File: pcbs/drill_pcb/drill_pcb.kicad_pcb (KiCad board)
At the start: 2 copper layers, 105 x 103 mm, 41 parts, among them J1 24V IN, J11 STEPPER STORAGE, J13 uC COMMUNICATION, J14 SERVO 1, J15 SERVO 2, J16 DEEP WEIGHT SENSOR, J17 SURFACE WEIGHT SENSOR, J2 DC MOTOR 24 V, J3 DC MOTOR UART, J4 ENCODER VERTICAL DRIVE, J5 LIMIT SENSOR TOP, J6 HEIGHT SENSOR, J7 STEPPER VERTICAL DRIVE, J8 ENCODER STORAGE, J9 LIMIT SENSOR BOTTOM, Q1 PMOS, U1 ESP32-DevKitC, U2 LM3940, U3 INA219BxD

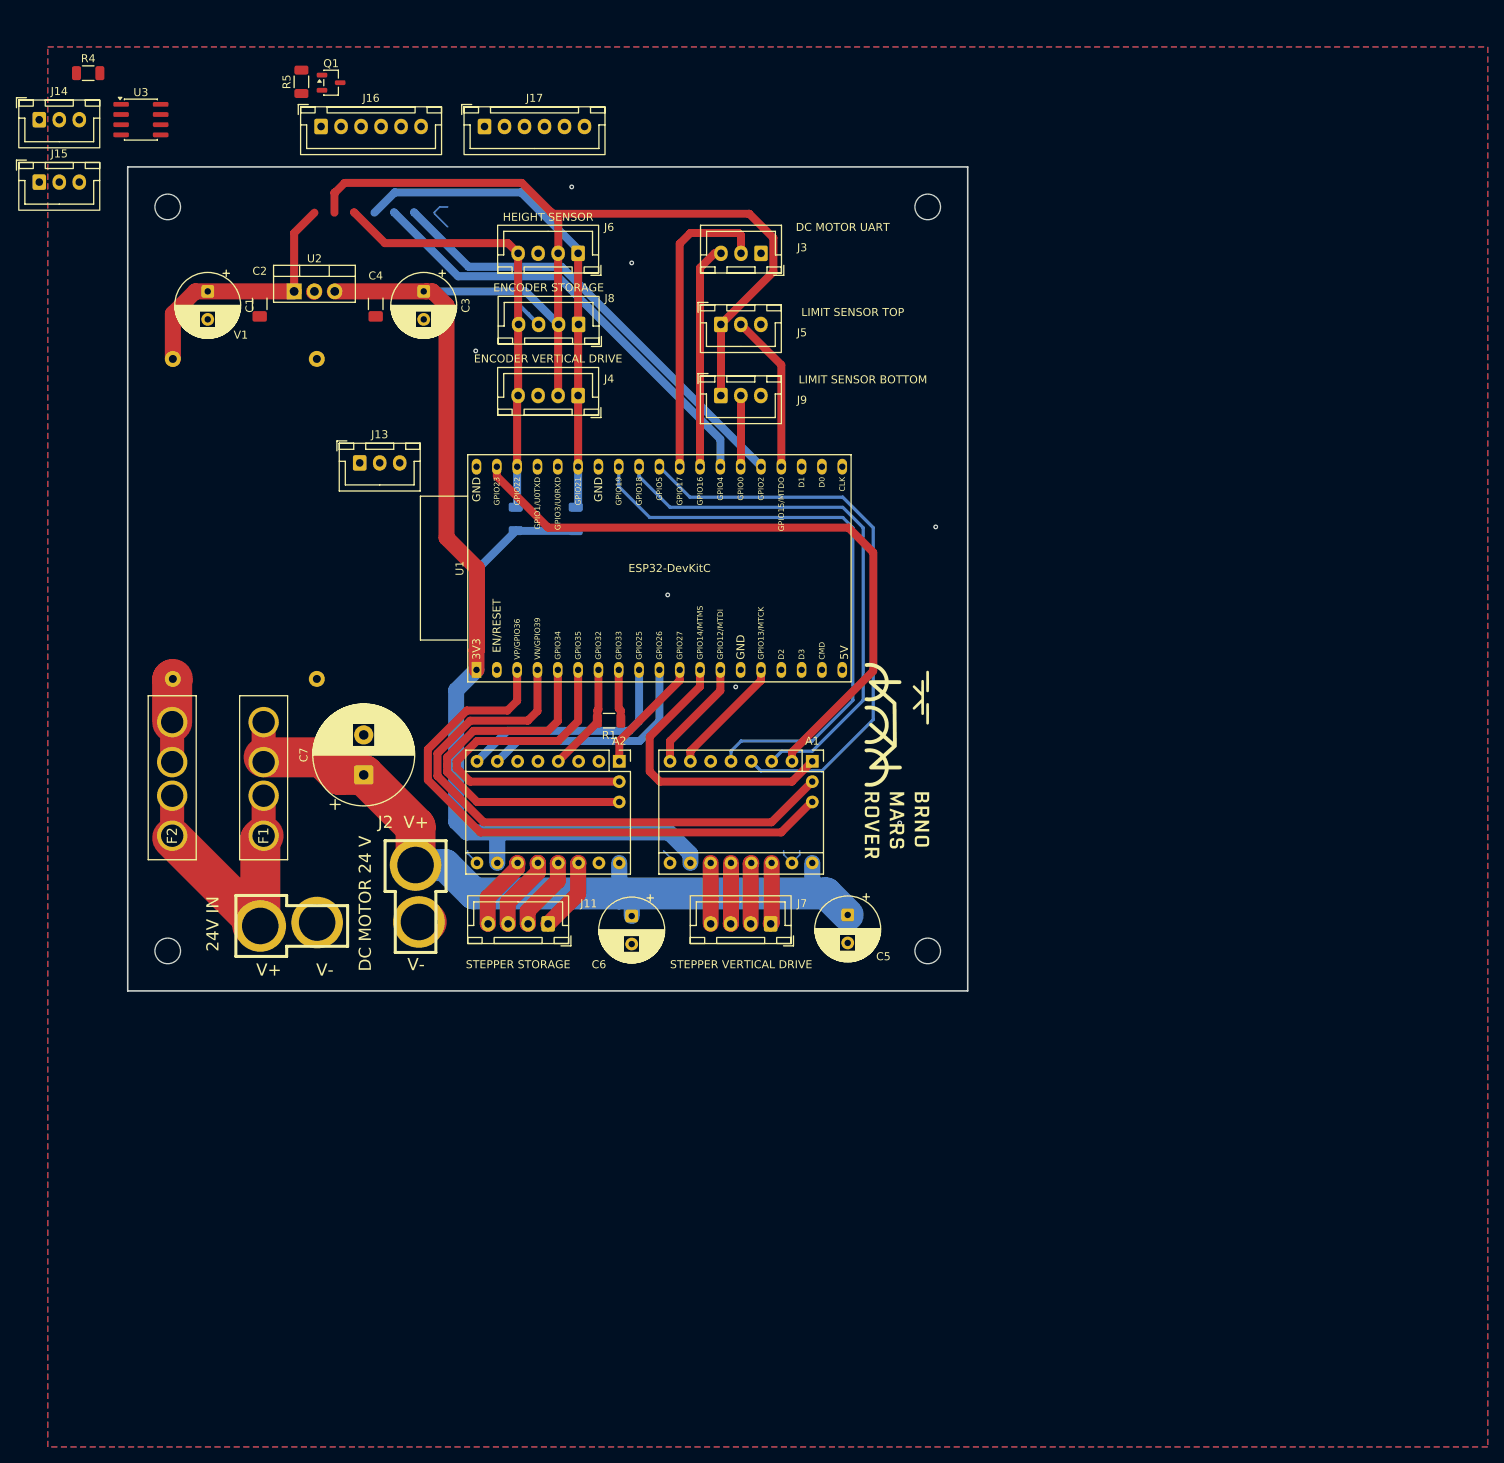
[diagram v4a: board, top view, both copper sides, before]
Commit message: Schematic changes: - Finalised the feature to turn off power for peripherals using a MOSFET. - Connected the stepper motor current sensor.
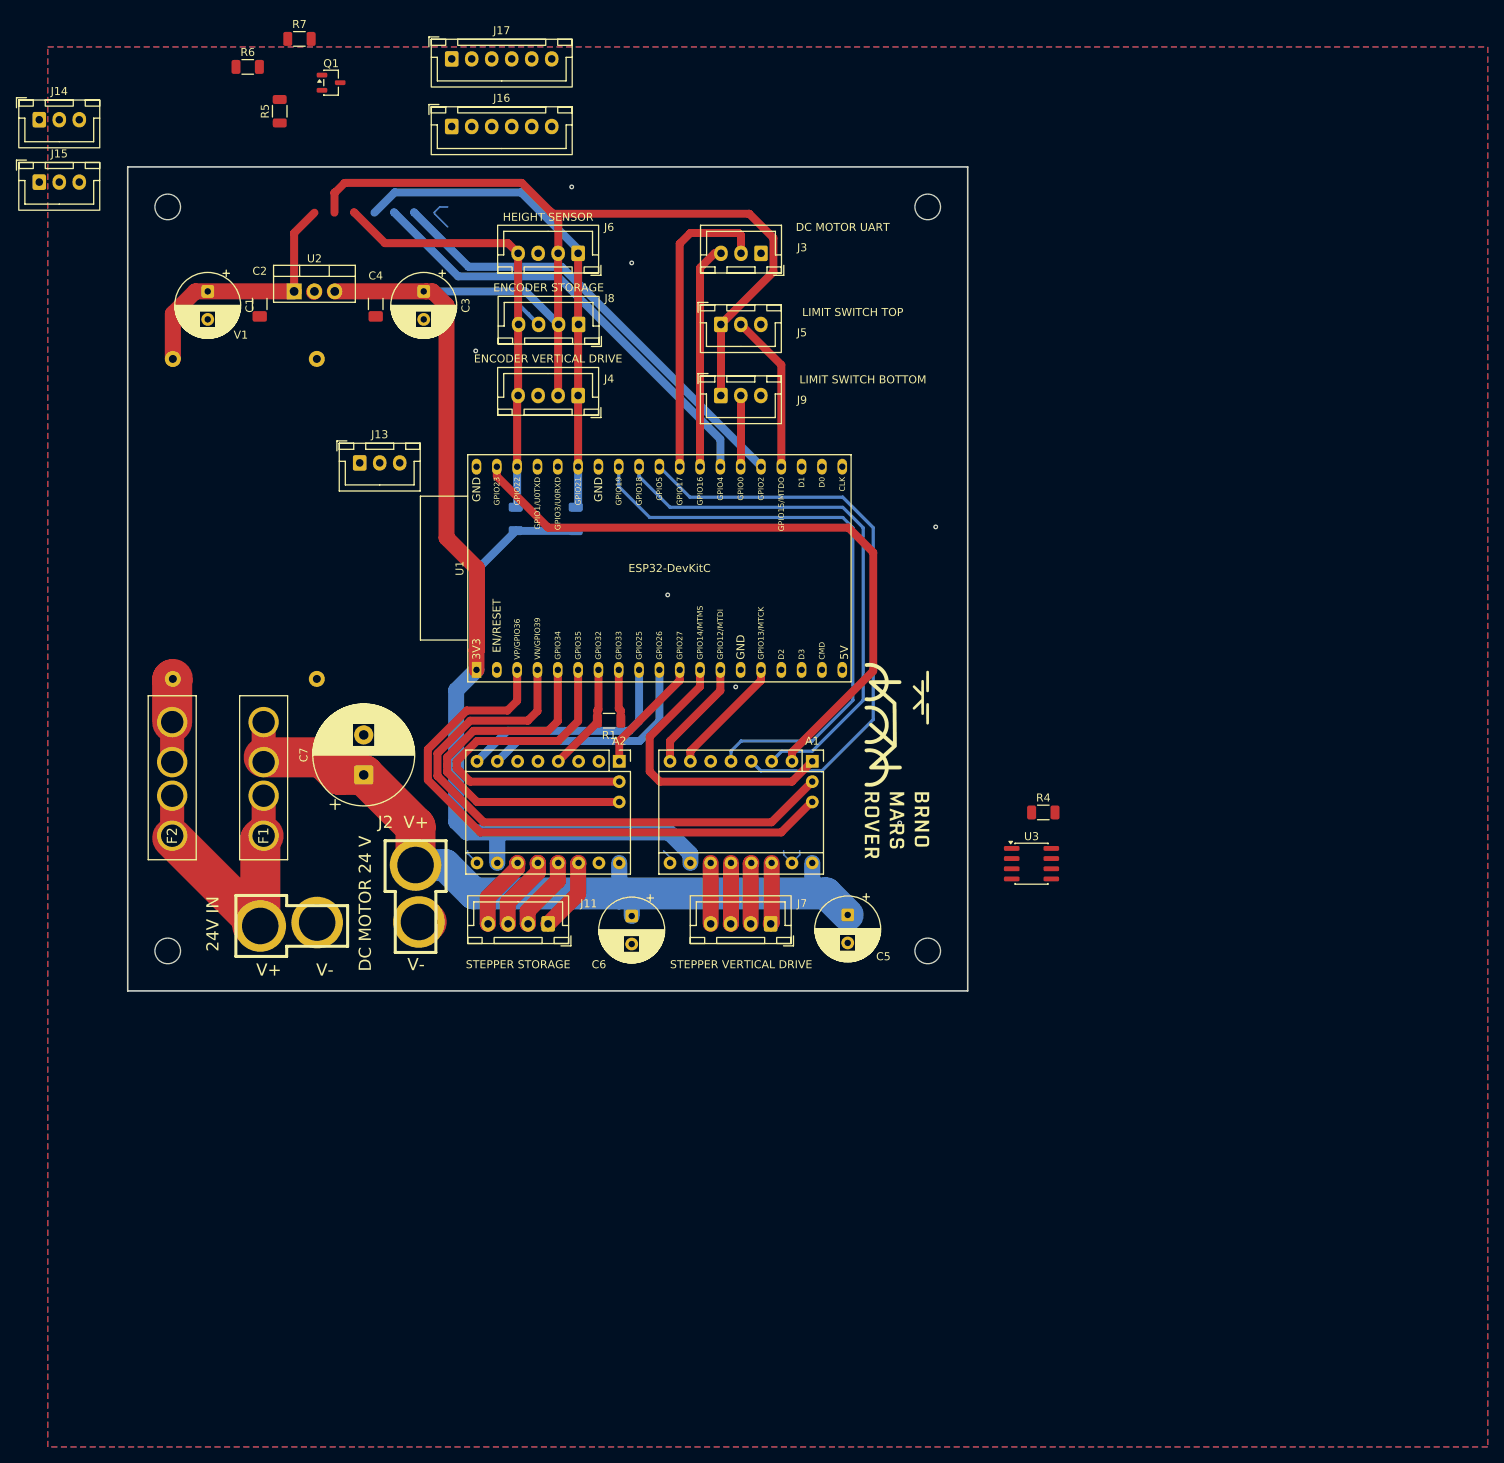
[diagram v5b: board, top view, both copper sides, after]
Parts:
- added R6: 100k, Resistor_SMD:R_1206_3216Metric, F.Cu at (45.0, 27.5)
- added R7: 1k, Resistor_SMD:R_1206_3216Metric, F.Cu at (51.5, 24.0)
- J5: value LIMIT SENSOR TOP -> LIMIT SWITCH TOP
- J9: value LIMIT SENSOR BOTTOM -> LIMIT SWITCH BOTTOM
- R4: value R -> R100
- R5: value R -> 100k
- moved R4 151.0 mm to (144.4, 120.7)
- moved U3 145.1 mm to (143.0, 127.1)
- moved J16 16.3 mm to (70.5, 35.0)
- moved J17 9.39 mm to (70.5, 26.5)
- moved R5 4.57 mm to (49.0, 33.0)
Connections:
- net LIMIT_SENSOR_BOTTOM renamed LIMIT_SWITCH_BOTTOM
- net LIMIT_SENSOR_TOP renamed LIMIT_SWITCH_TOP
- A1 pad 16: +24V -> Net-(A1-VM)
- C5 pad 1: +24V -> Net-(A1-VM)
- J16 pad 2: Net-(J16-Pin_2) -> RST
- J17 pad 2: Net-(J16-Pin_2) -> RST
- J4 pad 2: +3.3V -> +3.3VP
- J6 pad 2: +3.3V -> +3.3VP
- J8 pad 2: +3.3V -> +3.3VP
- Q1 pad 1: RST -> Net-(Q1-G)
- Q1 pad 3: Net-(J16-Pin_2) -> +3.3VP
- R4 pad 1: unconnected-(R4-Pad1) -> +24V
- R4 pad 2: unconnected-(R4-Pad2) -> Net-(A1-VM)
- R5 pad 2: RST -> Net-(Q1-G)
- U3 pad 5: +3.3V -> +3.3VP
- U3 pad 7: unconnected-(U3-IN--Pad7) -> Net-(A1-VM)
- U3 pad 8: unconnected-(U3-IN+-Pad8) -> +24V
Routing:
- net LIMIT_SWITCH_TOP: track 65.4 -> 0.00 mm
- net LIMIT_SWITCH_BOTTOM: track 55.9 -> 0.00 mm
- net unconnected-(A2-DIAG1-Pad18): track 0.00 -> 47.0 mm
- net unconnected-(A2-DIAG0-Pad17): track 0.00 -> 45.5 mm
- net unconnected-(U1-MTDO/GPIO15/ADC2_CH3-Pad23): track 0.00 -> 19.9 mm
- net unconnected-(U1-GPIO0/BOOT/ADC2_CH1-Pad25): track 0.00 -> 8.91 mm

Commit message: added servo capacitors
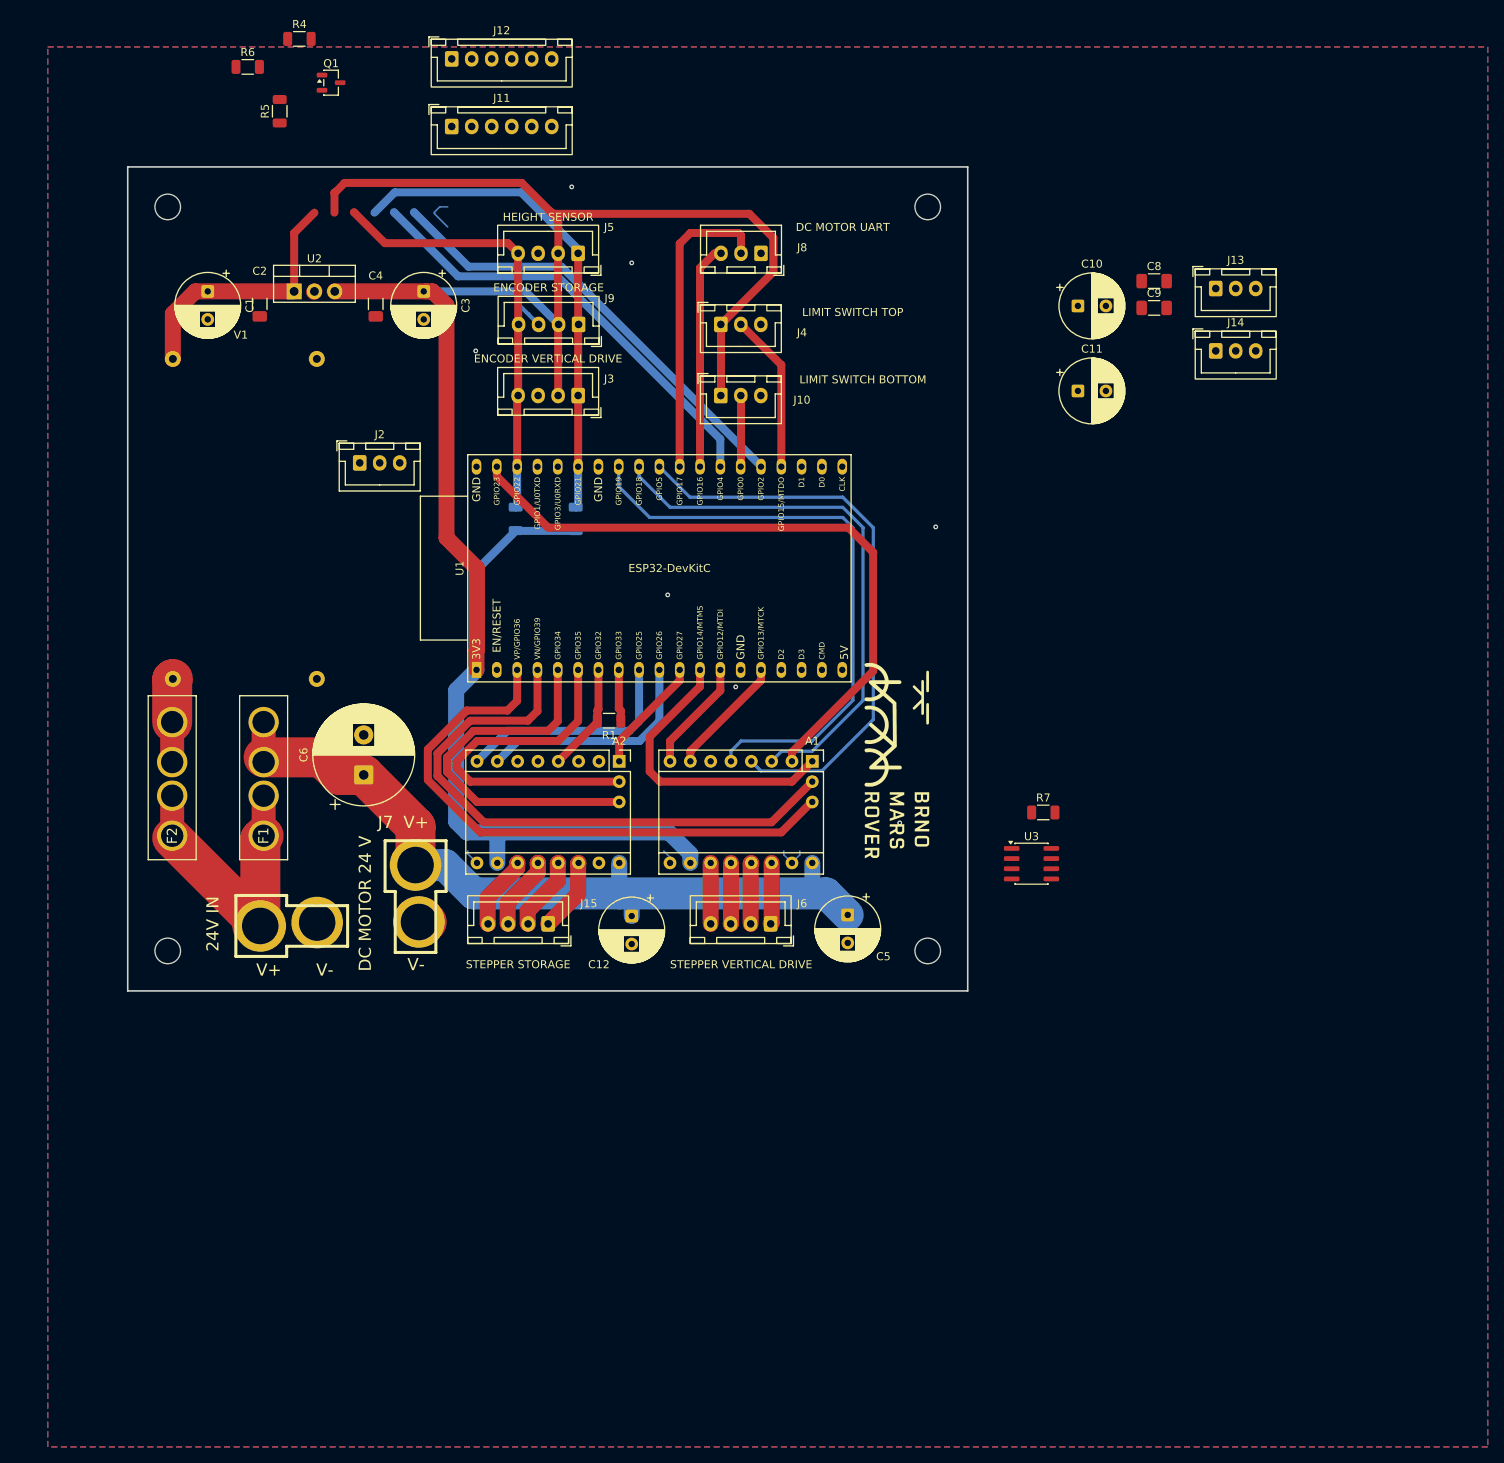
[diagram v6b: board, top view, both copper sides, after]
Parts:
- added C10: 470μ, Capacitor_THT:CP_Radial_D8.0mm_P3.50mm, F.Cu at (148.8, 57.4)
- added C11: 470μ, Capacitor_THT:CP_Radial_D8.0mm_P3.50mm, F.Cu at (148.8, 68.0)
- added C8: 100n, Capacitor_SMD:C_1206_3216Metric_Pad1.33x1.80mm_HandSolder, F.Cu at (158.3, 54.3)
- added C9: 100n, Capacitor_SMD:C_1206_3216Metric_Pad1.33x1.80mm_HandSolder, F.Cu at (158.3, 57.6)
- moved J13 148.6 mm to (166.0, 55.2)
- moved J14 148.6 mm to (166.0, 63.0)
- renumbered C6 to C12, C7 to C6, J9 to J10, J16 to J11, J17 to J12, J14 to J13, J15 to J14, J11 to J15, J13 to J2, J4 to J3, J5 to J4, J6 to J5, J7 to J6, J2 to J7, J3 to J8, J8 to J9, R7 to R4, R4 to R7

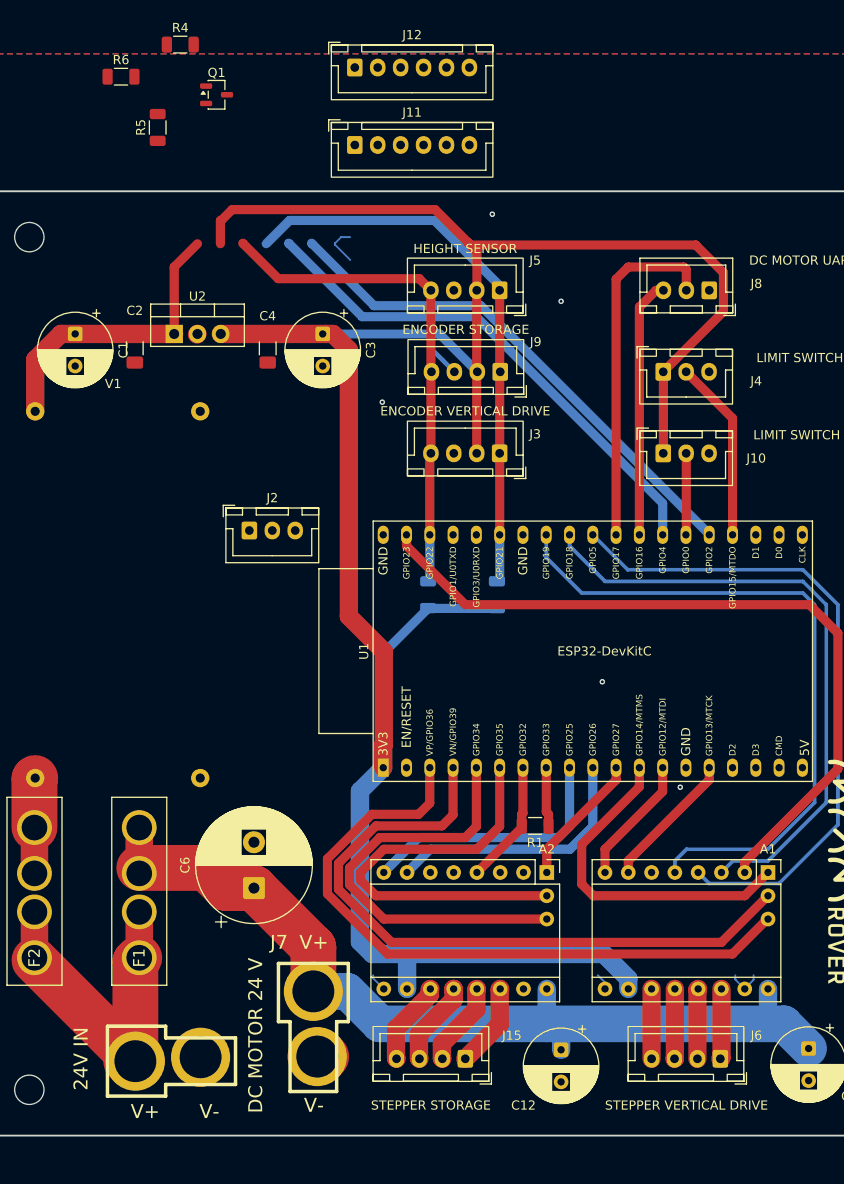
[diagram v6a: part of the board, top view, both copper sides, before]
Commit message: ADC's wired up, layout commented
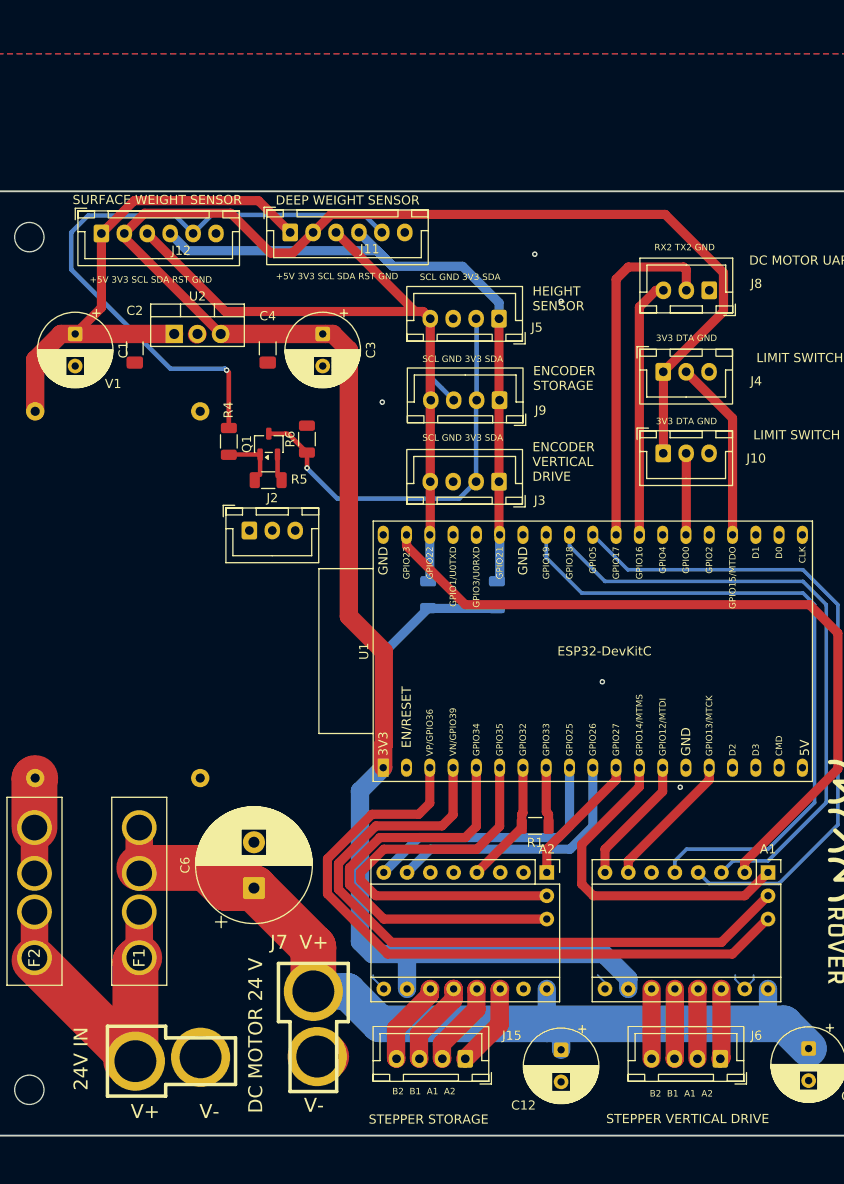
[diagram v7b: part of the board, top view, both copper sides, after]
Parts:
- moved R6 44.4 mm to (65.3, 67.0), turned to 90 degrees
- moved R4 43.6 mm to (56.8, 67.3), turned to -90 degrees
- moved R5 40.3 mm to (61.0, 71.5), turned to 180 degrees
- moved Q1 38.5 mm to (61.1, 67.6), turned to 90 degrees
- moved J12 33.0 mm to (42.9, 44.6)
- moved J11 11.9 mm to (63.5, 44.5)
- moved J5 3.10 mm to (86.2, 53.9)
- moved J3 3.10 mm to (86.2, 71.7)
- moved J9 3.10 mm to (86.3, 62.8)
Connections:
- J11 pad 2: RST -> +3.3V
- J11 pad 5: ADC_DEEP_RST -> RST
- J12 pad 2: RST -> +3.3V
- J12 pad 5: ADC_DEEP_RST -> RST
- U1 pad 23: unconnected-(U1-MTDO/GPIO15/ADC2_CH3-Pad23) -> SERVO2_PWM
- U1 pad 26: unconnected-(U1-ADC2_CH0/GPIO4-Pad26) -> SERVO1_PWM
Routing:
- net RST: track 0.00 -> 69.0 mm, vias 0 -> 1
- net ADC_DEEP_RST: track 56.6 -> 0.06 mm
- net unconnected-(U1-ADC2_CH0/GPIO4-Pad26): track 56.0 -> 0.00 mm
- net +3.3VP: track 0.00 -> 45.2 mm, vias 0 -> 1
- net +5V: track 32.9 -> 57.6 mm
- net SCL1: track 54.5 -> 75.9 mm
- net unconnected-(U1-MTDO/GPIO15/ADC2_CH3-Pad23): track 19.9 -> 0.00 mm
- net (no net): track 0.00 -> 19.9 mm
- net SDA1: track 61.8 -> 75.3 mm
- net +3.3V: track 271.1 -> 257.9 mm
- net Net-(Q1-G): track 0.00 -> 6.46 mm
- net GND: track 16.3 -> 11.9 mm
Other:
- board text added: "+5V 3V3 SCL SDA RST GND"
- board text added: "3V3 DTA GND"
- board text added: "B2 B1 A1 A2"
- board text added: "ENCODER STORAGE"
- board text added: "ENCODER VERTICAL DRIVE"
- board text added: "HEIGHT SENSOR"
- board text added: "RX2 TX2 GND"
- board text added: "SCL GND 3V3 SDA"
